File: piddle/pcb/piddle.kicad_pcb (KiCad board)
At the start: 2 copper layers, 133.5 x 118 mm, 68 parts, among them J1 Conn_01x03_Socket, J10 Conn_01x03_Socket, J11 Conn_01x02_Socket, J12 Conn_01x02_Socket, J13 Conn_01x02_Pin, J2 Conn_01x03_Socket, J3 Conn_01x03_Socket, J4 Conn_01x03_Socket, J5 Conn_01x03_Socket, J7 Conn_01x03_Socket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

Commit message: Change data line resistor values
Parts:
- R1, R10, R2, R3, R4, R5, R6, R7, R8, R9: value 200 -> 400
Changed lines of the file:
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@@
         (effects (font (size 1 1) (thickness 0.15)))
     )
-    (fp_text value "200" (at 5.08 2.37 -162) (layer "F.Fab")
+    (fp_text value "400" (at 5.08 2.37 -162) (layer "F.Fab")
         (effects (font (size 1 1) (thickness 0.15)))
     )
@@
         (effects (font (size 1 1) (thickness 0.15)))
     )
-    (fp_text value "200" (at 5.08 2.37 -126) (layer "F.Fab")
+    (fp_text value "400" (at 5.08 2.37 -126) (layer "F.Fab")
         (effects (font (size 1 1) (thickness 0.15)))
     )
@@
         (effects (font (size 1 1) (thickness 0.15)))
     )
-    (fp_text value "200" (at 5.08 2.37 162) (layer "F.Fab")
+    (fp_text value "400" (at 5.08 2.37 162) (layer "F.Fab")
         (effects (font (size 1 1) (thickness 0.15)))
     )
@@
         (effects (font (size 1 1) (thickness 0.15)))
     )
-    (fp_text value "200" (at 5.08 2.37 -36) (layer "F.Fab")
+    (fp_text value "400" (at 5.08 2.37 -36) (layer "F.Fab")
         (effects (font (size 1 1) (thickness 0.15)))
     )
@@
         (effects (font (size 1 1) (thickness 0.15)))
     )
-    (fp_text value "200" (at 5.08 2.37 126) (layer "F.Fab")
+    (fp_text value "400" (at 5.08 2.37 126) (layer "F.Fab")
         (effects (font (size 1 1) (thickness 0.15)))
     )
@@
         (effects (font (size 1 1) (thickness 0.15)))
     )
-    (fp_text value "200" (at 5.08 2.37 90) (layer "F.Fab")
+    (fp_text value "400" (at 5.08 2.37 90) (layer "F.Fab")
         (effects (font (size 1 1) (thickness 0.15)))
     )
@@
         (effects (font (size 1 1) (thickness 0.15)))
     )
-    (fp_text value "200" (at 5.08 2.37 162) (layer "F.Fab")
+    (fp_text value "400" (at 5.08 2.37 162) (layer "F.Fab")
         (effects (font (size 1 1) (thickness 0.15)))
     )
@@
         (effects (font (size 1 1) (thickness 0.15)))
     )
-    (fp_text value "200" (at 3.58 2.37 90) (layer "F.Fab")
+    (fp_text value "400" (at 3.58 2.37 90) (layer "F.Fab")
         (effects (font (size 1 1) (thickness 0.15)))
     )
@@
         (effects (font (size 1 1) (thickness 0.15)))
     )
-    (fp_text value "200" (at 5.08 2.37 -162) (layer "F.Fab")
+    (fp_text value "400" (at 5.08 2.37 -162) (layer "F.Fab")
         (effects (font (size 1 1) (thickness 0.15)))
     )
@@
         (effects (font (size 1 1) (thickness 0.15)))
     )
-    (fp_text value "200" (at 5.08 2.37 126) (layer "F.Fab")
-        (effects (font (size 1 1) (thickness 0.15)))
-    )
+    (fp_text value "400" (at 5.08 2.37 126) (layer "F.Fab")
+        (effects (font (size 1 1) (thickness 0.15)))
+    )

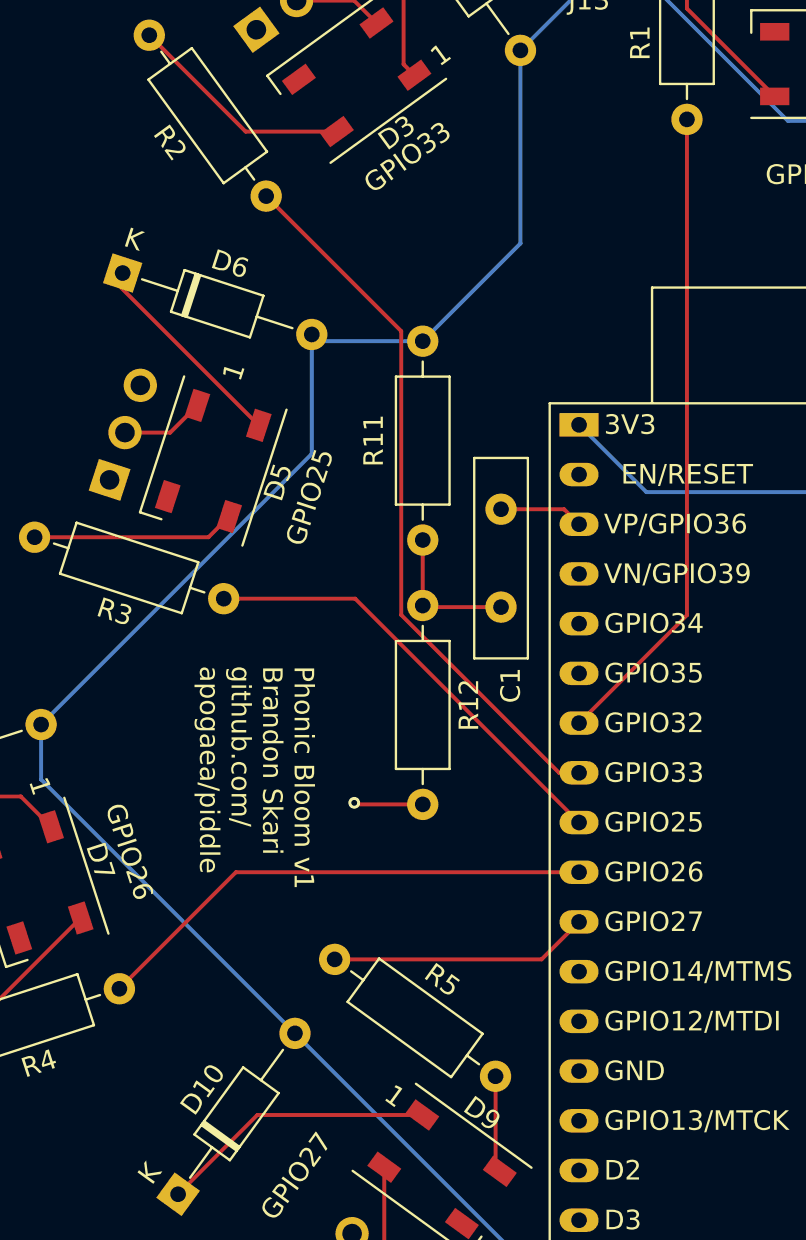
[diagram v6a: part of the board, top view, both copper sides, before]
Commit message: Change LED pins so they work with WLED
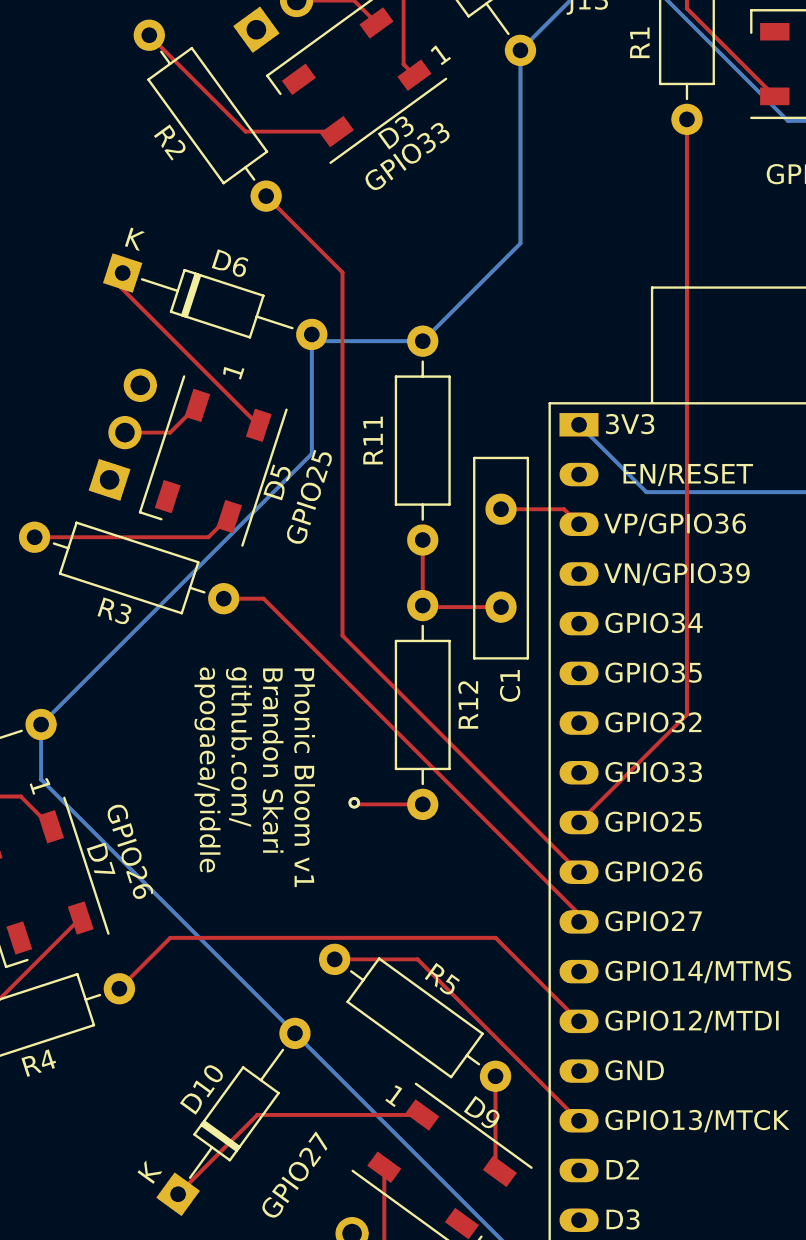
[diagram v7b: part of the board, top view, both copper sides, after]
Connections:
- R1 pad 1: /GPIO32 -> /GPIO25
- R2 pad 1: /GPIO33 -> /GPIO26
- R3 pad 1: /GPIO25 -> /GPIO27
- R4 pad 1: /GPIO26 -> /GPIO12
- R5 pad 1: /GPIO27 -> /GPIO13
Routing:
- net /GPIO33: track 36.7 -> 0.00 mm
- net /GPIO32: track 33.1 -> 0.00 mm
- net /GPIO12: track 0.00 -> 26.3 mm
- net /GPIO13: track 0.00 -> 15.9 mm
- net /GPIO25: track 22.9 -> 38.2 mm
- net /GPIO26: track 26.0 -> 41.2 mm
- net /GPIO27: track 13.3 -> 25.2 mm
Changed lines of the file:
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@@
       (stroke (width 0.1) (type solid)) (layer "F.Fab"))
     (pad "1" thru_hole circle (at 0 0 162) (size 1.6 1.6) (drill 0.8) (layers "*.Cu" "*.Mask")
-      (net 7 "/GPIO25") (pintype "passive"))
+      (net 9 "/GPIO27") (pintype "passive"))
     (pad "2" thru_hole oval (at 10.16 0 162) (size 1.6 1.6) (drill 0.8) (layers "*.Cu" "*.Mask")
       (net 69 "Net-(D5-DIN)") (pintype "passive"))
@@
       (stroke (width 0.1) (type solid)) (layer "F.Fab"))
     (pad "1" thru_hole circle (at 0 0 324) (size 1.6 1.6) (drill 0.8) (layers "*.Cu" "*.Mask")
-      (net 9 "/GPIO27") (pintype "passive"))
+      (net 13 "/GPIO13") (pintype "passive"))
     (pad "2" thru_hole oval (at 10.16 0 324) (size 1.6 1.6) (drill 0.8) (layers "*.Cu" "*.Mask")
       (net 71 "Net-(D9-DIN)") (pintype "passive"))
@@
       (stroke (width 0.1) (type solid)) (layer "F.Fab"))
     (pad "1" thru_hole circle (at 0 0 126) (size 1.6 1.6) (drill 0.8) (layers "*.Cu" "*.Mask")
-      (net 41 "/GPIO33") (pintype "passive"))
+      (net 8 "/GPIO26") (pintype "passive"))
     (pad "2" thru_hole oval (at 10.16 0 126) (size 1.6 1.6) (drill 0.8) (layers "*.Cu" "*.Mask")
       (net 68 "Net-(D3-DIN)") (pintype "passive"))
@@
       (stroke (width 0.1) (type solid)) (layer "F.Fab"))
     (pad "1" thru_hole circle (at 0 0 90) (size 1.6 1.6) (drill 0.8) (layers "*.Cu" "*.Mask")
-      (net 38 "/GPIO32") (pintype "passive"))
+      (net 7 "/GPIO25") (pintype "passive"))
     (pad "2" thru_hole oval (at 10.16 0 90) (size 1.6 1.6) (drill 0.8) (layers "*.Cu" "*.Mask")
       (net 67 "Net-(D1-DIN)") (pintype "passive"))
@@
       (stroke (width 0.1) (type solid)) (layer "F.Fab"))
     (pad "1" thru_hole circle (at 0 0 198) (size 1.6 1.6) (drill 0.8) (layers "*.Cu" "*.Mask")
-      (net 8 "/GPIO26") (pintype "passive"))
+      (net 11 "/GPIO12") (pintype "passive"))
     (pad "2" thru_hole oval (at 10.16 0 198) (size 1.6 1.6) (drill 0.8) (layers "*.Cu" "*.Mask")
       (net 70 "Net-(D7-DIN)") (pintype "passive"))
@@
   (segment (start 91.833623 96.596343) (end 92.6 97.36272) (width 0.2) (layer "F.Cu") (net 3))
   (segment (start 88.61328 96.596343) (end 91.833623 96.596343) (width 0.2) (layer "F.Cu") (net 3))
-  (segment (start 81.163429 101.166149) (end 92.6 112.60272) (width 0.2) (layer "F.Cu") (net 7))
-  (segment (start 74.444647 101.166149) (end 81.163429 101.166149) (width 0.2) (layer "F.Cu") (net 7))
-  (segment (start 69.11328 121.096343) (end 75.066903 115.14272) (width 0.2) (layer "F.Cu") (net 8))
-  (segment (start 75.066903 115.14272) (end 92.6 115.14272) (width 0.2) (layer "F.Cu") (net 8))
-  (segment (start 80.11328 119.596343) (end 90.686377 119.596343) (width 0.2) (layer "F.Cu") (net 9))
-  (segment (start 90.686377 119.596343) (end 92.6 117.68272) (width 0.2) (layer "F.Cu") (net 9))
+  (segment (start 98.11328 107.08944) (end 92.6 112.60272) (width 0.2) (layer "F.Cu") (net 7))
+  (segment (start 98.11328 76.676343) (end 98.11328 107.08944) (width 0.2) (layer "F.Cu") (net 7))
+  (segment (start 80.51328 84.496343) (end 80.51328 103.056) (width 0.2) (layer "F.Cu") (net 8))
+  (segment (start 76.61328 80.596343) (end 80.51328 84.496343) (width 0.2) (layer "F.Cu") (net 8))
+  (segment (start 80.51328 103.056) (end 92.6 115.14272) (width 0.2) (layer "F.Cu") (net 8))
+  (segment (start 76.483429 101.166149) (end 74.444647 101.166149) (width 0.2) (layer "F.Cu") (net 9))
+  (segment (start 92.6 117.68272) (end 92.6 117.28272) (width 0.2) (layer "F.Cu") (net 9))
+  (segment (start 92.6 117.28272) (end 76.483429 101.166149) (width 0.2) (layer "F.Cu") (net 9))
+  (segment (start 69.11328 121.096343) (end 71.71328 118.496343) (width 0.2) (layer "F.Cu") (net 11))
+  (segment (start 71.71328 118.496343) (end 88.333623 118.496343) (width 0.2) (layer "F.Cu") (net 11))
+  (segment (start 88.333623 118.496343) (end 92.6 122.76272) (width 0.2) (layer "F.Cu") (net 11))
   (segment (start 79.28734 88.008843) (end 78.944647 87.66615) (width 0.2) (layer "B.Cu") (net 12))
   (segment (start 78.944647 87.66615) (end 78.944647 93.764976) (width 0.2) (layer "B.Cu") (net 12))
@@
   (segment (start 89.606254 83.015869) (end 84.61328 88.008843) (width 0.2) (layer "B.Cu") (net 12))
   (segment (start 65.11328 110.404832) (end 78.085178 123.37673) (width 0.2) (layer "B.Cu") (net 12))
+  (segment (start 84.353623 119.596343) (end 92.6 127.84272) (width 0.2) (layer "F.Cu") (net 13))
+  (segment (start 80.11328 119.596343) (end 84.353623 119.596343) (width 0.2) (layer "F.Cu") (net 13))
   (segment (start 112.11328 128.64944) (end 118 122.76272) (width 0.2) (layer "F.Cu") (net 23))
   (segment (start 112.11328 144.336343) (end 112.11328 128.64944) (width 0.2) (layer "F.Cu") (net 23))
@@
   (segment (start 99.30328 70.246343) (end 94.11328 65.056343) (width 0.2) (layer "B.Cu") (net 37))
   (segment (start 107.69328 69.096343) (end 106.54328 70.246343) (width 0.2) (layer "B.Cu") (net 37))
-  (segment (start 92.6 107.52272) (end 98.11328 102.00944) (width 0.2) (layer "F.Cu") (net 38))
-  (segment (start 98.11328 102.00944) (end 98.11328 76.676343) (width 0.2) (layer "F.Cu") (net 38))
   (segment (start 83.634356 64.931634) (end 83.634356 73.864421) (width 0.2) (layer "F.Cu") (net 39))
   (segment (start 83.634356 73.864421) (end 84.189691 74.419756) (width 0.2) (layer "F.Cu") (net 39))
   (segment (start 78.168183 70.603368) (end 81.103368 70.603368) (width 0.2) (layer "F.Cu") (net 40))
   (segment (start 81.103368 70.603368) (end 82.25 71.75) (width 0.2) (layer "F.Cu") (net 40))
-  (segment (start 76.61328 80.596343) (end 83.51328 87.496343) (width 0.2) (layer "F.Cu") (net 41))
-  (segment (start 83.51328 101.996343) (end 91.579657 110.06272) (width 0.2) (layer "F.Cu") (net 41))
-  (segment (start 91.579657 110.06272) (end 92.6 110.06272) (width 0.2) (layer "F.Cu") (net 41))
-  (segment (start 83.51328 87.496343) (end 83.51328 101.996343) (width 0.2) (layer "F.Cu") (net 41))
   (segment (start 69.281913 84.526537) (end 69.183086 84.526537) (width 0.2) (layer "F.Cu") (net 42))
   (segment (start 69.11328 84.596343) (end 69.11328 85.187246) (width 0.2) (layer "F.Cu") (net 42))
